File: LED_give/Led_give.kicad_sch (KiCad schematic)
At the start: 20 parts, among them J1 DG141R-2.54-02P-14-00, J2 DG142R-5.08-04P-14, J3 DG142R-5.08-02P-14, Q1 50N06, Q2 50N06, Q3 50N06

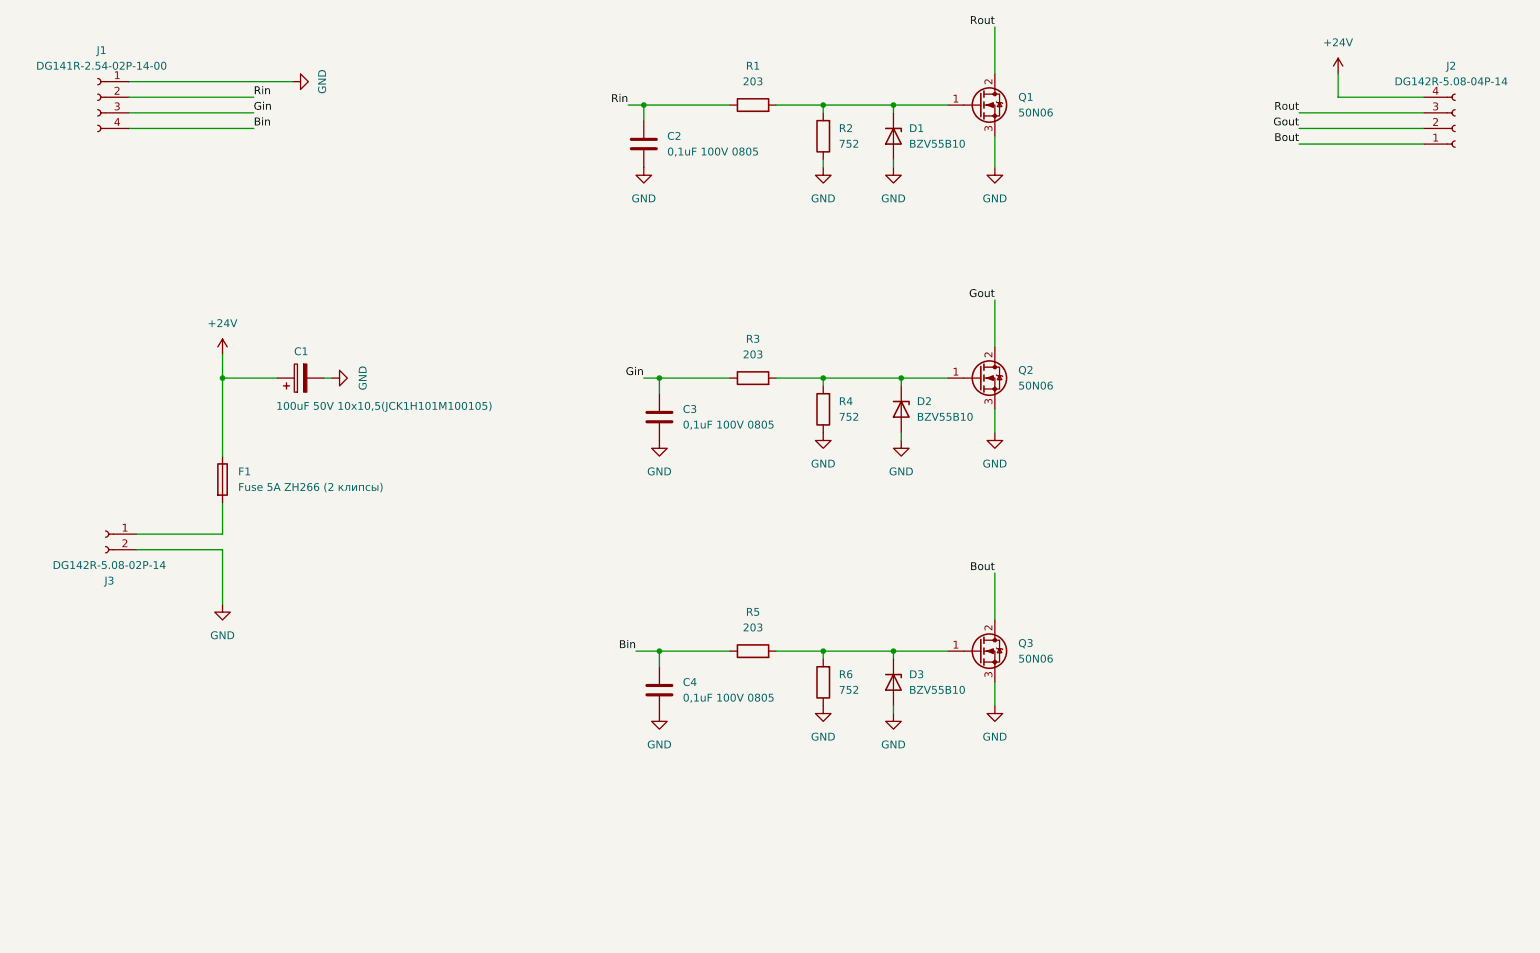
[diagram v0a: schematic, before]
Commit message: add LED_give PCB
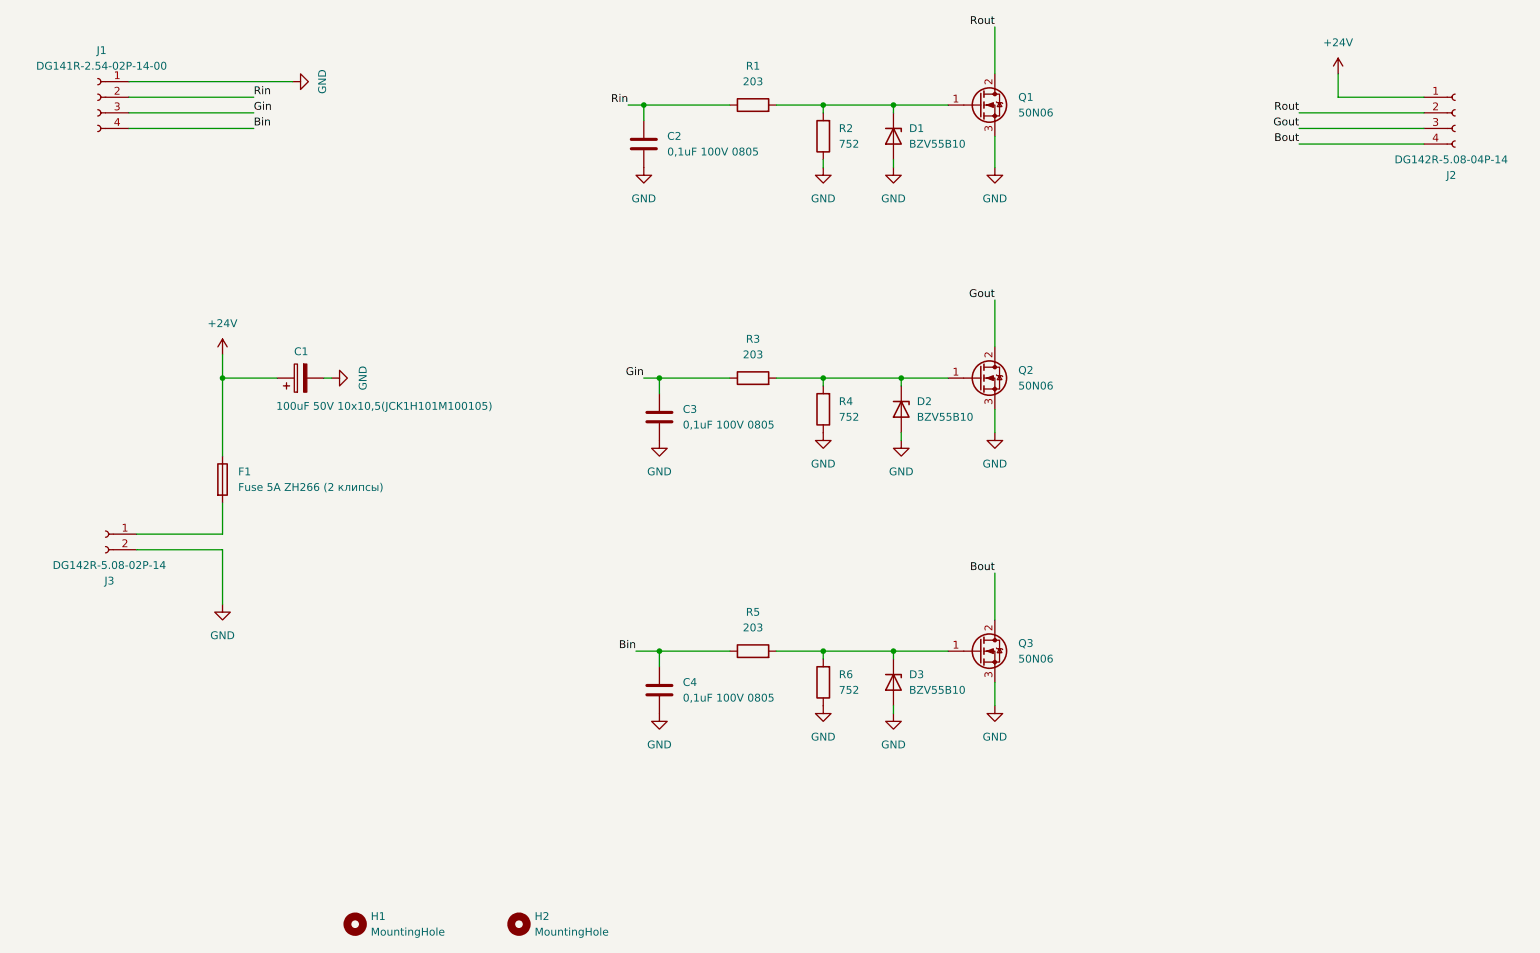
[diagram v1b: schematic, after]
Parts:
- added H1, H2: MountingHole, MountingHole:MountingHole_3.2mm_M3_Pad, symbol Mechanical:MountingHole
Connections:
- net +24V: now also J2.1 (Pin_1); no longer J2.4 (Pin_4)
- net Bout: now also J2.4 (Pin_4); no longer J2.1 (Pin_1)
- net Gout: now also J2.3 (Pin_3); no longer J2.2 (Pin_2)
- net Rout: now also J2.2 (Pin_2); no longer J2.3 (Pin_3)
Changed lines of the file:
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@@
 	(symbol
 		(lib_id "Connector:Conn_01x04_Socket")
-		(at 257.81 49.53 0)
-		(mirror x)
-		(unit 1)
-		(exclude_from_sim no)
-		(in_bom yes)
-		(on_board yes)
-		(dnp no)
-		(fields_autoplaced yes)
+		(at 257.81 46.99 0)
+		(unit 1)
+		(exclude_from_sim no)
+		(in_bom yes)
+		(on_board yes)
+		(dnp no)
 		(property "Reference" "J2"
-			(at 257.175 39.37 0)
+			(at 257.175 57.15 0)
 			(effects
 				(font
@@
 		)
 		(property "Value" "DG142R-5.08-04P-14"
-			(at 257.175 41.91 0)
+			(at 257.175 54.61 0)
 			(effects
 				(font
@@
 		)
 		(property "Footprint" "Connector:DG142R-5.08-04P-14"
-			(at 257.81 49.53 0)
+			(at 257.81 46.99 0)
 			(effects
 				(font
@@
 		)
 		(property "Datasheet" "~"
-			(at 257.81 49.53 0)
+			(at 257.81 46.99 0)
 			(effects
 				(font
@@
 		)
 		(property "Description" "Generic connector, single row, 01x04, script generated"
-			(at 257.81 49.53 0)
+			(at 257.81 46.99 0)
 			(effects
 				(font
@@
 	)
 	(symbol
+		(lib_id "Mechanical:MountingHole")
+		(at 105.41 179.07 0)
+		(unit 1)
+		(exclude_from_sim yes)
+		(in_bom no)
+		(on_board yes)
+		(dnp no)
+		(fields_autoplaced yes)
+		(property "Reference" "H2"
+			(at 107.95 177.7999 0)
+			(effects
+				(font
+					(size 1.27 1.27)
+				)
+				(justify left)
+			)
+		)
+		(property "Value" "MountingHole"
+			(at 107.95 180.3399 0)
+			(effects
+				(font
+					(size 1.27 1.27)
+				)
+				(justify left)
+			)
+		)
+		(property "Footprint" "MountingHole:MountingHole_3.2mm_M3_Pad"
+			(at 105.41 179.07 0)
+			(effects
+				(font
+					(size 1.27 1.27)
+				)
+				(hide yes)
+			)
+		)
+		(property "Datasheet" "~"
+			(at 105.41 179.07 0)
+			(effects
+				(font
+					(size 1.27 1.27)
+				)
+				(hide yes)
+			)
+		)
+		(property "Description" "Mounting Hole without connection"
+			(at 105.41 179.07 0)
+			(effects
+				(font
+					(size 1.27 1.27)
+				)
+				(hide yes)
+			)
+		)
+		(instances
+			(project "Led_give"
+				(path "/8eff6871-f756-4cb1-95e6-ab8a99d05362"
+					(reference "H2")
+					(unit 1)
+				)
+			)
+		)
+	)
+	(symbol
 		(lib_id "Device:C")
 		(at 128.27 140.97 0)
@@
 					(unit 1)
 				)
+			)
+		)
+	)
+	(symbol
+		(lib_id "Mechanical:MountingHole")
+		(at 78.74 179.07 0)
+		(unit 1)
+		(exclude_from_sim yes)
+		(in_bom no)
+		(on_board yes)
+		(dnp no)
+		(fields_autoplaced yes)
+		(property "Reference" "H1"
+			(at 81.28 177.7999 0)
+			(effects
+				(font
+					(size 1.27 1.27)
+				)
+				(justify left)
+			)
+		)
+		(property "Value" "MountingHole"
+			(at 81.28 180.3399 0)
+			(effects
+				(font
+					(size 1.27 1.27)
+				)
+				(justify left)
+			)
+		)
+		(property "Footprint" "MountingHole:MountingHole_3.2mm_M3_Pad"
+			(at 78.74 179.07 0)
+			(effects
+				(font
+					(size 1.27 1.27)
+				)
+				(hide yes)
+			)
+		)
+		(property "Datasheet" "~"
+			(at 78.74 179.07 0)
+			(effects
+				(font
+					(size 1.27 1.27)
+				)
+				(hide yes)
+			)
+		)
+		(property "Description" "Mounting Hole without connection"
+			(at 78.74 179.07 0)
+			(effects
+				(font
+					(size 1.27 1.27)
+				)
+				(hide yes)
+			)
+		)
+		(instances
+			(project ""
+				(path "/8eff6871-f756-4cb1-95e6-ab8a99d05362"
+					(reference "H1")
+					(unit 1)
+				)
